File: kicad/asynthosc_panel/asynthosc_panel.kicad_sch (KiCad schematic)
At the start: 13 parts, among them J15 Conn_02x04_Odd_Even

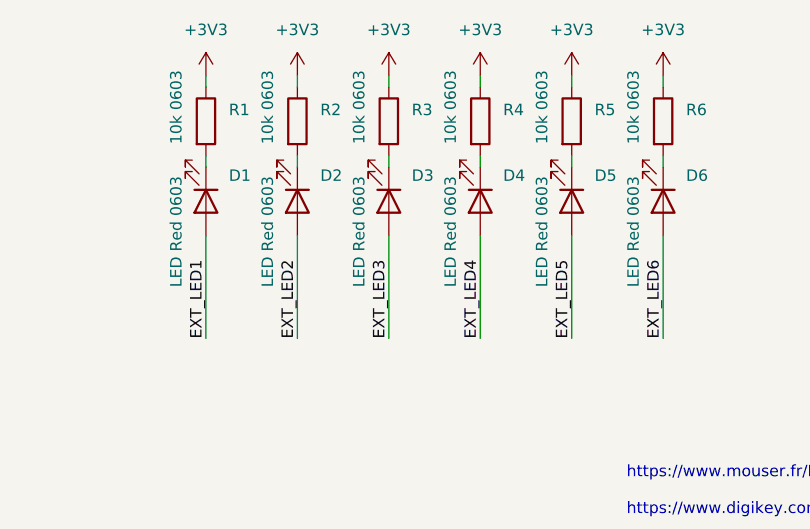
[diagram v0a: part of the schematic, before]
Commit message: [SCH] Update LED model
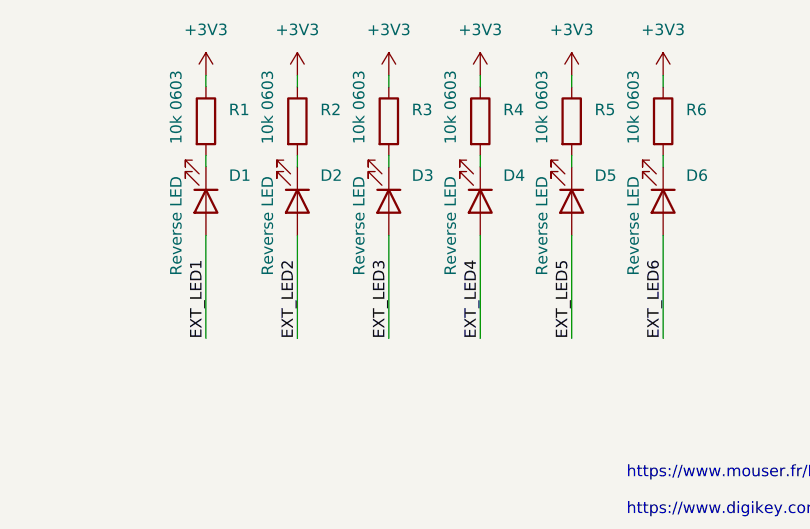
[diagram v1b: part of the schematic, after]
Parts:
- D1, D2, D3, D4, D5, D6: value LED Red 0603 -> Reverse LED; footprint LED_SMD:LED_0603_1608Metric_Pad1.05x0.95mm_HandSolder -> asynthosc:LED_Sunled_XZxx45x-9_nohole; Manufacturer (none) -> SunLED; RefNum (none) -> XZxx45x-9
- J15: Manufacturer Boomele -> (none)
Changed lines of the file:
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@@
 			)
 		)
-		(property "Value" "LED Red 0603"
+		(property "Value" "Reverse LED"
 			(at 113.538 39.116 0)
 			(show_name no)
@@
 			)
 		)
-		(property "Footprint" "LED_SMD:LED_0603_1608Metric_Pad1.05x0.95mm_HandSolder"
+		(property "Footprint" "asynthosc:LED_Sunled_XZxx45x-9_nohole"
 			(at 116.84 41.91 0)
 			(hide yes)
@@
 		(property "Sim.Pins" "1=K 2=A"
 			(at 116.84 41.91 0)
+			(hide yes)
+			(show_name no)
+			(do_not_autoplace no)
+			(effects
+				(font
+					(size 1.27 1.27)
+				)
+			)
+		)
+		(property "Manufacturer" "SunLED"
+			(at 116.84 41.91 90)
+			(hide yes)
+			(show_name no)
+			(do_not_autoplace no)
+			(effects
+				(font
+					(size 1.27 1.27)
+				)
+			)
+		)
+		(property "RefNum" "XZxx45x-9"
+			(at 116.84 41.91 90)
 			(hide yes)
 			(show_name no)
@@
 			)
 		)
-		(property "Value" "LED Red 0603"
+		(property "Value" "Reverse LED"
 			(at 103.378 39.116 0)
 			(show_name no)
@@
 			)
 		)
-		(property "Footprint" "LED_SMD:LED_0603_1608Metric_Pad1.05x0.95mm_HandSolder"
+		(property "Footprint" "asynthosc:LED_Sunled_XZxx45x-9_nohole"
 			(at 106.68 41.91 0)
 			(hide yes)
@@
 		(property "Sim.Pins" "1=K 2=A"
 			(at 106.68 41.91 0)
+			(hide yes)
+			(show_name no)
+			(do_not_autoplace no)
+			(effects
+				(font
+					(size 1.27 1.27)
+				)
+			)
+		)
+		(property "Manufacturer" "SunLED"
+			(at 106.68 41.91 90)
+			(hide yes)
+			(show_name no)
+			(do_not_autoplace no)
+			(effects
+				(font
+					(size 1.27 1.27)
+				)
+			)
+		)
+		(property "RefNum" "XZxx45x-9"
+			(at 106.68 41.91 90)
 			(hide yes)
 			(show_name no)
@@
 			)
 		)
-		(property "Manufacturer" "Boomele "
+		(property "Manufacturer" ""
 			(at 57.15 40.64 0)
 			(hide yes)
@@
 			)
 		)
-		(property "Value" "LED Red 0603"
+		(property "Value" "Reverse LED"
 			(at 123.698 39.116 0)
 			(show_name no)
@@
 			)
 		)
-		(property "Footprint" "LED_SMD:LED_0603_1608Metric_Pad1.05x0.95mm_HandSolder"
+		(property "Footprint" "asynthosc:LED_Sunled_XZxx45x-9_nohole"
 			(at 127 41.91 0)
 			(hide yes)
@@
 		(property "Sim.Pins" "1=K 2=A"
 			(at 127 41.91 0)
+			(hide yes)
+			(show_name no)
+			(do_not_autoplace no)
+			(effects
+				(font
+					(size 1.27 1.27)
+				)
+			)
+		)
+		(property "Manufacturer" "SunLED"
+			(at 127 41.91 90)
+			(hide yes)
+			(show_name no)
+			(do_not_autoplace no)
+			(effects
+				(font
+					(size 1.27 1.27)
+				)
+			)
+		)
+		(property "RefNum" "XZxx45x-9"
+			(at 127 41.91 90)
 			(hide yes)
 			(show_name no)
@@
 			)
 		)
-		(property "Value" "LED Red 0603"
+		(property "Value" "Reverse LED"
 			(at 154.178 39.116 0)
 			(show_name no)
@@
 			)
 		)
-		(property "Footprint" "LED_SMD:LED_0603_1608Metric_Pad1.05x0.95mm_HandSolder"
+		(property "Footprint" "asynthosc:LED_Sunled_XZxx45x-9_nohole"
 			(at 157.48 41.91 0)
 			(hide yes)
@@
 		(property "Sim.Pins" "1=K 2=A"
 			(at 157.48 41.91 0)
+			(hide yes)
+			(show_name no)
+			(do_not_autoplace no)
+			(effects
+				(font
+					(size 1.27 1.27)
+				)
+			)
+		)
+		(property "Manufacturer" "SunLED"
+			(at 157.48 41.91 90)
+			(hide yes)
+			(show_name no)
+			(do_not_autoplace no)
+			(effects
+				(font
+					(size 1.27 1.27)
+				)
+			)
+		)
+		(property "RefNum" "XZxx45x-9"
+			(at 157.48 41.91 90)
 			(hide yes)
 			(show_name no)
@@
 			)
 		)
-		(property "Value" "LED Red 0603"
+		(property "Value" "Reverse LED"
 			(at 144.018 39.116 0)
 			(show_name no)
@@
 			)
 		)
-		(property "Footprint" "LED_SMD:LED_0603_1608Metric_Pad1.05x0.95mm_HandSolder"
+		(property "Footprint" "asynthosc:LED_Sunled_XZxx45x-9_nohole"
 			(at 147.32 41.91 0)
 			(hide yes)
@@
 		(property "Sim.Pins" "1=K 2=A"
 			(at 147.32 41.91 0)
+			(hide yes)
+			(show_name no)
+			(do_not_autoplace no)
+			(effects
+				(font
+					(size 1.27 1.27)
+				)
+			)
+		)
+		(property "Manufacturer" "SunLED"
+			(at 147.32 41.91 90)
+			(hide yes)
+			(show_name no)
+			(do_not_autoplace no)
+			(effects
+				(font
+					(size 1.27 1.27)
+				)
+			)
+		)
+		(property "RefNum" "XZxx45x-9"
+			(at 147.32 41.91 90)
 			(hide yes)
 			(show_name no)
@@
 			)
 		)
-		(property "Value" "LED Red 0603"
+		(property "Value" "Reverse LED"
 			(at 133.858 39.116 0)
 			(show_name no)
@@
 			)
 		)
-		(property "Footprint" "LED_SMD:LED_0603_1608Metric_Pad1.05x0.95mm_HandSolder"
+		(property "Footprint" "asynthosc:LED_Sunled_XZxx45x-9_nohole"
 			(at 137.16 41.91 0)
 			(hide yes)
@@
 			(hide yes)
 			(show_name no)
+			(do_not_autoplace no)
+			(effects
+				(font
+					(size 1.27 1.27)
+				)
+			)
+		)
+		(property "Manufacturer" "SunLED"
+			(at 137.16 41.91 90)
+			(hide yes)
+			(show_name no)
+			(do_not_autoplace no)
+			(effects
+				(font
+					(size 1.27 1.27)
+				)
+			)
+		)
+		(property "RefNum" "XZxx45x-9"
+			(at 137.16 41.91 90)
+			(hide yes)
+			(show_name no)

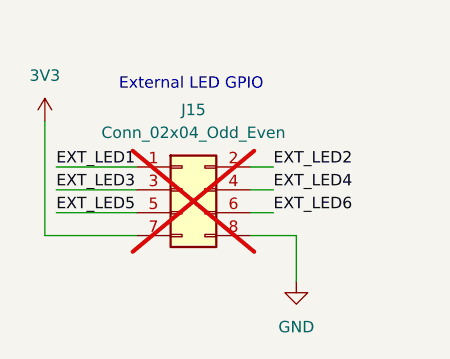
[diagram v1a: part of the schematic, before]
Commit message: [PANEL] Decorative stuff
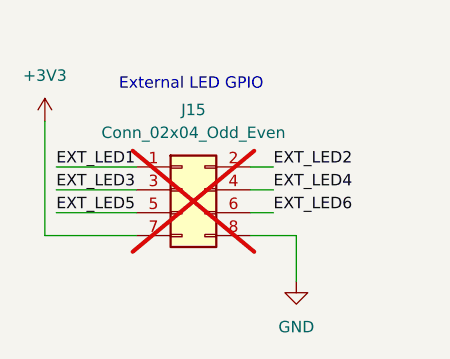
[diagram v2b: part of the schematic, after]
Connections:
- net 3V3 is gone; now on net +3V3: J15.7 (Pin_7)
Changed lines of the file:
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@@
 			)
 		)
-		(property "Value" "3V3"
+		(property "Value" "+3V3"
 			(at 41.91 27.94 0)
 			(show_name no)
